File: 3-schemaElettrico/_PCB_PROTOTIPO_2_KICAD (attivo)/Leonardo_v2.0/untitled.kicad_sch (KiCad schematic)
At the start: 0 parts

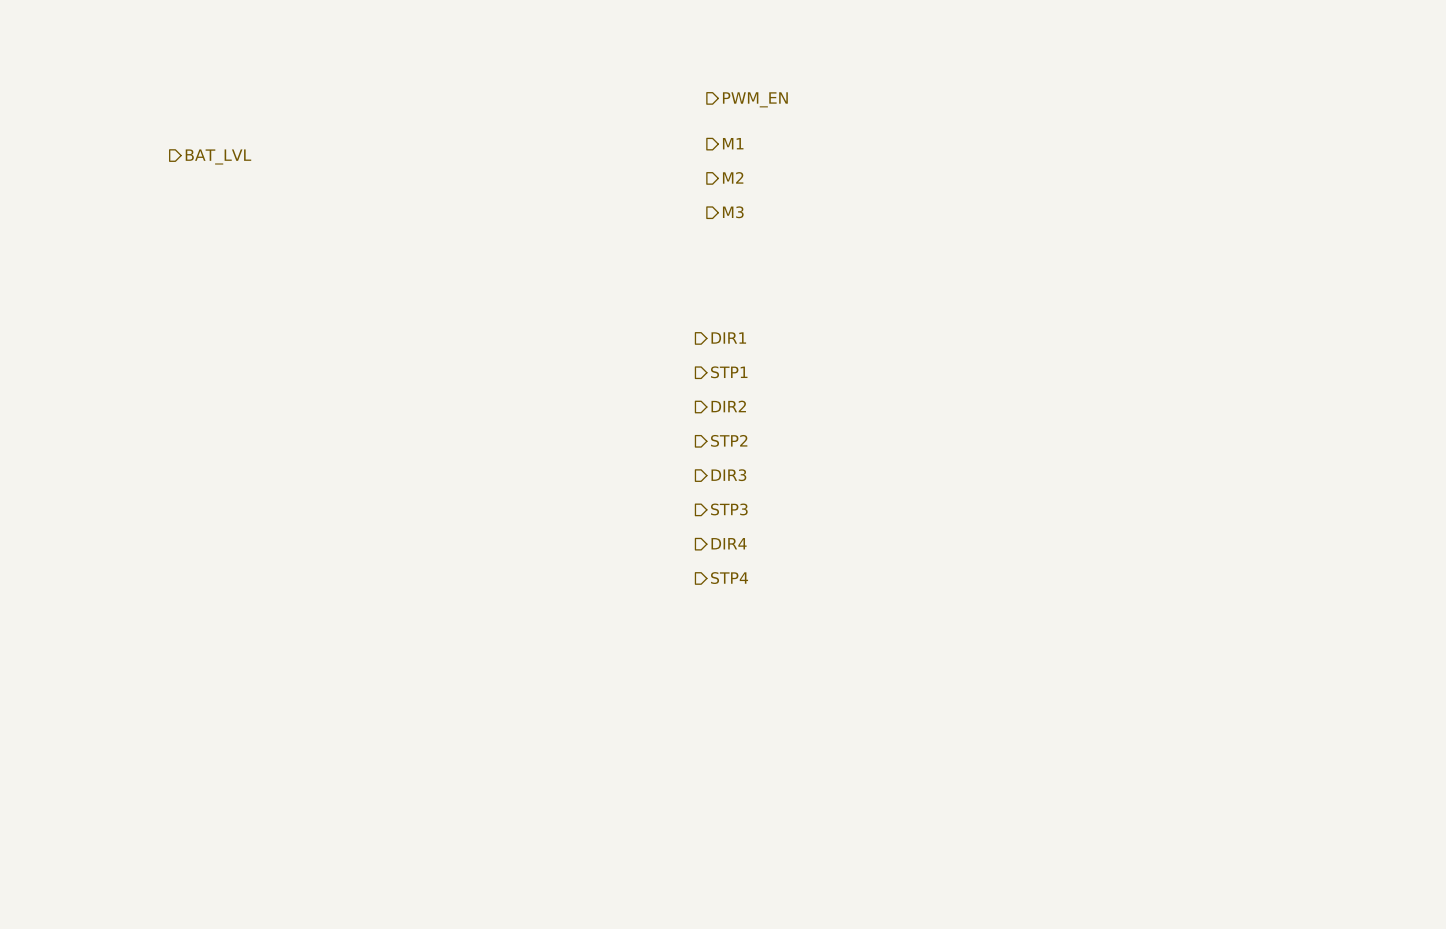
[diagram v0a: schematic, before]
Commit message: placed nodeMCU
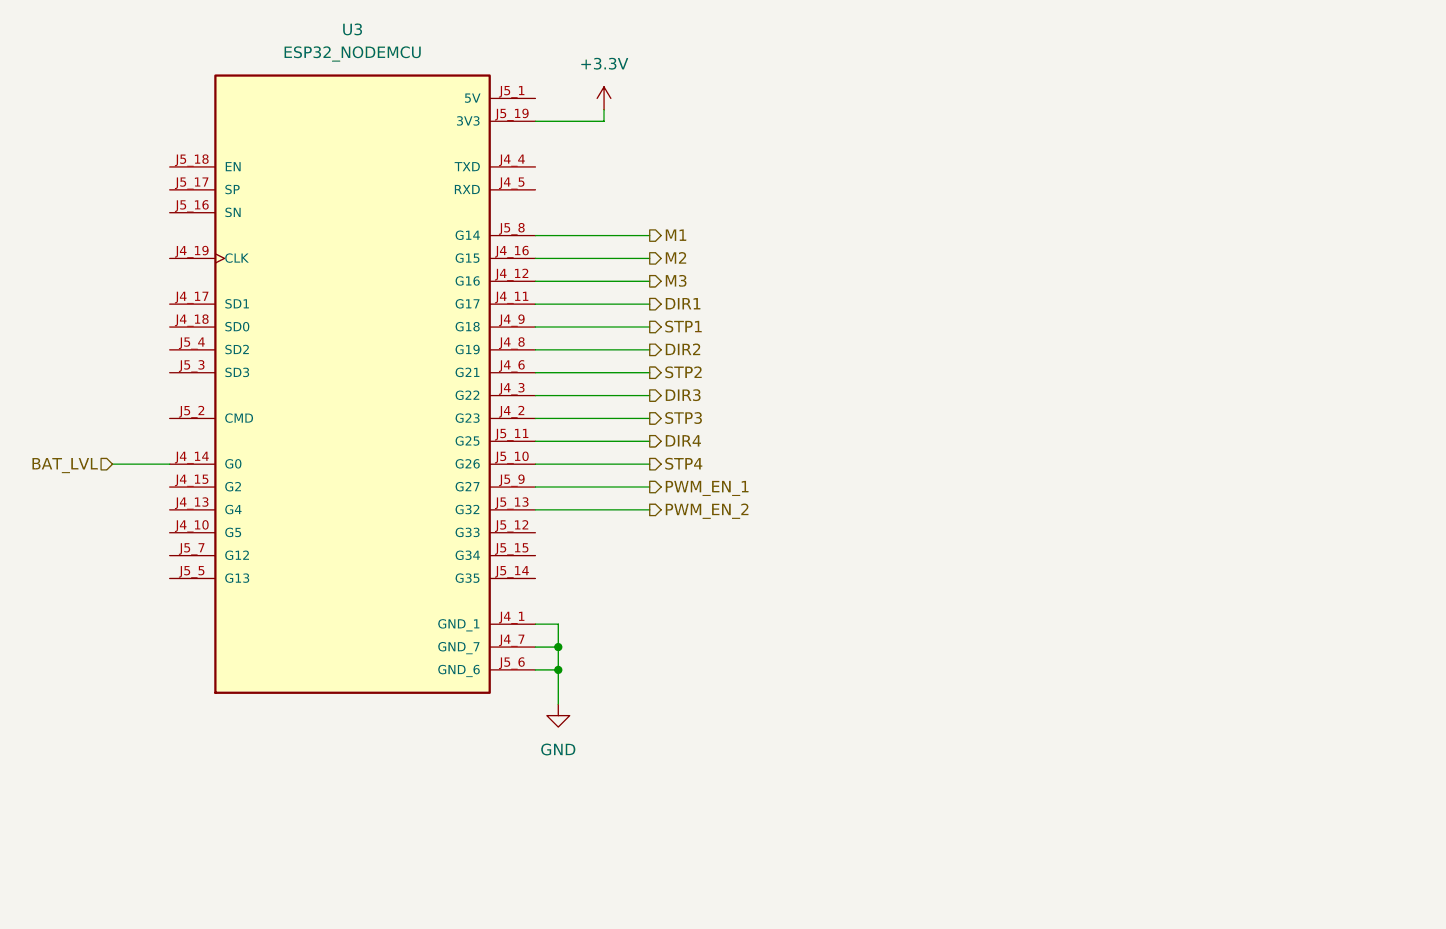
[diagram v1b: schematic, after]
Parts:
- added U3: ESP32_NODEMCU, ESP32_NODEMCU:MODULE_ESP32_NODEMCU, symbol ESP32_NODEMCU:ESP32_NODEMCU
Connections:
- net BAT_LVL: now also U3.J4_14 (G0)
- net DIR1: now also U3.J4_11 (G17)
- net DIR2: now also U3.J4_8 (G19)
- net DIR3: now also U3.J4_3 (G22)
- net DIR4: now also U3.J5_11 (G25)
- net M1: now also U3.J5_8 (G14)
- net M2: now also U3.J4_16 (G15)
- net M3: now also U3.J4_12 (G16)
- net STP1: now also U3.J4_9 (G18)
- net STP2: now also U3.J4_6 (G21)
- net STP3: now also U3.J4_2 (G23)
- net STP4: now also U3.J5_10 (G26)
- new net +3.3V: U3.J5_19 (3V3)
- new net GND: U3.J4_1 (GND_1), U3.J4_7 (GND_7), U3.J5_6 (GND_6)
- new net PWM_EN_1: U3.J5_9 (G27)
- new net PWM_EN_2: U3.J5_13 (G32)

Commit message: ok
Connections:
- net DIR1: now also U3.J4_8 (G19); no longer U3.J4_11 (G17)
- net DIR2: now also U3.J4_3 (G22); no longer U3.J4_8 (G19)
- net DIR3: now also U3.J5_11 (G25); no longer U3.J4_3 (G22)
- net DIR4: now also U3.J5_9 (G27); no longer U3.J5_11 (G25)
- net M1: now also U3.J4_12 (G16); no longer U3.J5_8 (G14)
- net M2: now also U3.J4_11 (G17); no longer U3.J4_16 (G15)
- net M3: now also U3.J4_9 (G18); no longer U3.J4_12 (G16)
- net PWM_EN_1: now also U3.J5_8 (G14); no longer U3.J5_9 (G27)
- net PWM_EN_2: now also U3.J4_16 (G15); no longer U3.J5_13 (G32)
- net STP1: now also U3.J4_6 (G21); no longer U3.J4_9 (G18)
- net STP2: now also U3.J4_2 (G23); no longer U3.J4_6 (G21)
- net STP3: now also U3.J5_10 (G26); no longer U3.J4_2 (G23)
- net STP4: now also U3.J5_13 (G32); no longer U3.J5_10 (G26)
- net speaker_out: now reaches U3.J4_15 (G2)
- net MS1: now reaches U3.J5_12 (G33)
- net MS3: now reaches U3.J5_14 (G35)
- net MS2: now reaches U3.J5_15 (G34)
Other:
- moved on the sheet: U3

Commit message: ok
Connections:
- net Buzzer: now reaches U3.J4_13 (G4)
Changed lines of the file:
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@@
+	(wire
+		(pts
+			(xy 106.68 109.22) (xy 127 109.22)
+		)
+		(stroke
+			(width 0)
+			(type default)
+		)
+	)
 	(wire
 		(pts
@@
 		)
 	)
+	(global_label "Buzzer"
+		(shape output)
+		(at 106.68 109.22 180)
+		(fields_autoplaced yes)
+		(effects
+			(font
+				(size 1.27 1.27)
+			)
+			(justify right)
+		)
+		(property "Intersheetrefs" "${INTERSHEET_REFS}"
+			(at 97.3448 109.22 0)
+			(effects
+				(font
+					(size 1.27 1.27)
+				)
+				(justify right)
+				(hide yes)
+			)
+		)
+	)

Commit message: semplificato
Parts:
- removed U3: ESP32_NODEMCU, ESP32_NODEMCU:MODULE_ESP32_NODEMCU, symbol ESP32_NODEMCU:ESP32_NODEMCU
- added R6, R7, R8: 10K, symbol Device:R_US
- added SW1: SW_DIP_x03, symbol Switch:SW_DIP_x03
- added U1: ~, symbol LIB_STE:NODEMCU-ESP32-38PIN
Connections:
- net +3.3V: now also R6.2, R7.2, R8.2, U1. (CLK)
- net BAT_LVL: now also U1. (CLK)
- net DIR1: now also U1. (CLK)
- net DIR2: now also U1. (CLK)
- net DIR3: now also U1. (CLK)
- net DIR4: now also U1. (CLK)
- net GND: now also SW1.1, SW1.2, SW1.3, U1. (CLK)
- net M1: now also R6.1, SW1.6
- net M2: now also R7.1, SW1.5
- net M3: now also R8.1, SW1.4
- net PWM_EN_1: now also U1. (CLK)
- net PWM_EN_2: now also U1. (CLK)
- net STP1: now also U1. (CLK)
- net STP2: now also U1. (CLK)
- net STP3: now also U1. (CLK)
- net STP4: now also U1. (CLK)
- new net LED: U1. (CLK)
- new net M1A: U1. (CLK)
- new net M1B: U1. (CLK)
- new net M1C: U1. (CLK)
- new net M1D: U1. (CLK)
- new net M2A: U1. (CLK)
- new net M2B: U1. (CLK)
- new net M2C: U1. (CLK)
- new net M2D: U1. (CLK)
- new net RX: U1. (CLK)
- new net TX: U1. (CLK)
- new net buzzer: U1. (CLK)

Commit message: OK
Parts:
- removed SW1: SW_DIP_x03, symbol Switch:SW_DIP_x03
- added J13: Conn_02x03_Odd_Even, Connector_PinHeader_2.54mm:PinHeader_2x03_P2.54mm_Vertical, symbol Connector_Generic:Conn_02x03_Odd_Even
- R6, R7, R8: footprint (none) -> Resistor_SMD:R_0805_2012Metric
- U1: footprint (none) -> ESP32_NODEMCU:DIP-38_1000_ELL
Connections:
- net +3.3V: now also U1.1 (3v3); no longer U1. (CLK)
- net BAT_LVL: now also U1.6 (G35); no longer U1. (CLK)
- net DIR1: now also U1.30 (G18); no longer U1. (CLK)
- net DIR2: now also U1.28 (G17); no longer U1. (CLK)
- net DIR3: now also U1.26 (G4); no longer U1. (CLK)
- net DIR4: now also U1.24 (G2); no longer U1. (CLK)
- net GND: now also U1.14 (GND), U1.32 (GND), U1.38 (GND), J13.1 (Pin_1), J13.3 (Pin_3), J13.5 (Pin_5); no longer U1. (CLK)
- net LED: now also U1.33 (G21); no longer U1. (CLK)
- net M1: now also R8.1, J13.6 (Pin_6); no longer R6.1
- net M1A: now also U1.7 (G32); no longer U1. (CLK)
- net M1B: now also U1.8 (G33); no longer U1. (CLK)
- net M1C: now also U1.9 (G25); no longer U1. (CLK)
- net M1D: now also U1.10 (G26); no longer U1. (CLK)
- net M2: now also J13.4 (Pin_4)
- net M2A: now also U1.11 (G27); no longer U1. (CLK)
- net M2B: now also U1.12 (G14); no longer U1. (CLK)
- net M2C: now also U1.13 (G12); no longer U1. (CLK)
- net M2D: now also U1.15 (G13); no longer U1. (CLK)
- net M3: now also R6.1, J13.2 (Pin_2); no longer R8.1
- net PWM_EN_1: now also U1.37 (G23); no longer U1. (CLK)
- net PWM_EN_2: now also U1.36 (G22); no longer U1. (CLK)
- net RX: now also U1.34 (RXD); no longer U1. (CLK)
- net STP1: now also U1.29 (G5); no longer U1. (CLK)
- net STP2: now also U1.27 (G16); no longer U1. (CLK)
- net STP3: now also U1.25 (G0); no longer U1. (CLK)
- net STP4: now also U1.23 (G15); no longer U1. (CLK)
- net TX: now also U1.35 (TXD); no longer U1. (CLK)
- net buzzer: now also U1.31 (G19); no longer U1. (CLK)

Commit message: OK
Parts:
- removed J13: Conn_02x03_Odd_Even, Connector_PinHeader_2.54mm:PinHeader_2x03_P2.54mm_Vertical, symbol Connector_Generic:Conn_02x03_Odd_Even
- removed R6, R7, R8: 10K, Resistor_SMD:R_0805_2012Metric, symbol Device:R_US
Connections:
- net BAT_LVL is gone; now on net M1B: U1.6 (G35)
- net M1A: now also U1.5 (G34); no longer U1.7 (G32)
- net M1B: no longer U1.8 (G33)
- net M1C: now also U1.7 (G32); no longer U1.9 (G25)
- net M1D: now also U1.8 (G33); no longer U1.10 (G26)
- net PWM_EN_1: now also U1.9 (G25); no longer U1.37 (G23)
- net PWM_EN_2: now also U1.10 (G26); no longer U1.36 (G22)
- net LED renamed FC2
- net buzzer renamed FC1
- new net FC3: U1.36 (G22)
- new net FC4: U1.37 (G23)
- no-connect marks 0 -> 10

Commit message: ok
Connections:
- net DIR1: now also U1.29 (G5); no longer U1.30 (G18)
- net DIR2: now also U1.27 (G16); no longer U1.28 (G17)
- net DIR3: now also U1.25 (G0); no longer U1.26 (G4)
- net DIR4: now also U1.23 (G15); no longer U1.24 (G2)
- net STP1: now also U1.30 (G18); no longer U1.29 (G5)
- net STP2: now also U1.28 (G17); no longer U1.27 (G16)
- net STP3: now also U1.26 (G4); no longer U1.25 (G0)
- net STP4: now also U1.24 (G2); no longer U1.23 (G15)
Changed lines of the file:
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@@
+	(wire
+		(pts
+			(xy 147.32 113.03) (xy 153.67 113.03)
+		)
+		(stroke
+			(width 0)
+			(type default)
+		)
+	)
+	(wire
+		(pts
+			(xy 147.32 85.09) (xy 153.67 85.09)
+		)
+		(stroke
+			(width 0)
+			(type default)
+		)
+	)
+	(wire
+		(pts
+			(xy 147.32 74.93) (xy 179.07 74.93)
+		)
+		(stroke
+			(width 0)
+			(type default)
+		)
+	)
+	(wire
+		(pts
+			(xy 147.32 102.87) (xy 153.67 102.87)
+		)
+		(stroke
+			(width 0)
+			(type default)
+		)
+	)
+	(wire
+		(pts
+			(xy 92.71 74.93) (xy 92.71 69.85)
+		)
+		(stroke
+			(width 0)
+			(type default)
+		)
+	)
+	(wire
+		(pts
+			(xy 111.76 90.17) (xy 119.38 90.17)
+		)
+		(stroke
+			(width 0)
+			(type default)
+		)
+	)
+	(wire
+		(pts
+			(xy 147.32 100.33) (xy 153.67 100.33)
+		)
+		(stroke
+			(width 0)
+			(type default)
+		)
+	)
+	(wire
+		(pts
+			(xy 179.07 90.17) (xy 179.07 95.25)
+		)
+		(stroke
+			(width 0)
+			(type default)
+		)
+	)
+	(wire
+		(pts
+			(xy 147.32 77.47) (xy 153.67 77.47)
+		)
+		(stroke
+			(width 0)
+			(type default)
+		)
+	)
+	(wire
+		(pts
+			(xy 92.71 109.22) (xy 92.71 107.95)
+		)
+		(stroke
+			(width 0)
+			(type default)
+		)
+	)
+	(wire
+		(pts
+			(xy 147.32 92.71) (xy 153.67 92.71)
+		)
+		(stroke
+			(width 0)
+			(type default)
+		)
+	)
+	(wire
+		(pts
+			(xy 111.76 100.33) (xy 119.38 100.33)
+		)
+		(stroke
+			(width 0)
+			(type default)
+		)
+	)
+	(wire
+		(pts
+			(xy 179.07 74.93) (xy 179.07 90.17)
+		)
+		(stroke
+			(width 0)
+			(type default)
+		)
+	)
+	(wire
+		(pts
+			(xy 147.32 87.63) (xy 153.67 87.63)
+		)
+		(stroke
+			(width 0)
+			(type default)
+		)
+	)
+	(wire
+		(pts
+			(xy 147.32 95.25) (xy 153.67 95.25)
+		)
+		(stroke
+			(width 0)
+			(type default)
+		)
+	)
+	(wire
+		(pts
+			(xy 147.32 107.95) (xy 153.67 107.95)
+		)
+		(stroke
+			(width 0)
+			(type default)
+		)
+	)
+	(wire
+		(pts
+			(xy 111.76 95.25) (xy 119.38 95.25)
+		)
+		(stroke
+			(width 0)
+			(type default)
+		)
+	)
+	(wire
+		(pts
+			(xy 111.76 102.87) (xy 119.38 102.87)
+		)
+		(stroke
+			(width 0)
+			(type default)
+		)
+	)
 	(wire
 		(pts
@@
 	(wire
 		(pts
-			(xy 147.32 85.09) (xy 153.67 85.09)
-		)
-		(stroke
-			(width 0)
-			(type default)
-		)
-	)
-	(wire
-		(pts
-			(xy 147.32 74.93) (xy 179.07 74.93)
-		)
-		(stroke
-			(width 0)
-			(type default)
-		)
-	)
-	(wire
-		(pts
-			(xy 92.71 74.93) (xy 92.71 69.85)
-		)
-		(stroke
-			(width 0)
-			(type default)
-		)
-	)
-	(wire
-		(pts
-			(xy 111.76 90.17) (xy 119.38 90.17)
-		)
-		(stroke
-			(width 0)
-			(type default)
-		)
-	)
-	(wire
-		(pts
-			(xy 179.07 90.17) (xy 179.07 95.25)
+			(xy 111.76 85.09) (xy 119.38 85.09)
 		)
 		(stroke
@@
 	(wire
 		(pts
-			(xy 147.32 77.47) (xy 153.67 77.47)
-		)
-		(stroke
-			(width 0)
-			(type default)
-		)
-	)
-	(wire
-		(pts
-			(xy 147.32 100.33) (xy 153.67 100.33)
-		)
-		(stroke
-			(width 0)
-			(type default)
-		)
-	)
-	(wire
-		(pts
-			(xy 147.32 113.03) (xy 153.67 113.03)
-		)
-		(stroke
-			(width 0)
-			(type default)
-		)
-	)
-	(wire
-		(pts
-			(xy 92.71 109.22) (xy 92.71 107.95)
-		)
-		(stroke
-			(width 0)
-			(type default)
-		)
-	)
-	(wire
-		(pts
-			(xy 147.32 107.95) (xy 153.67 107.95)
-		)
-		(stroke
-			(width 0)
-			(type default)
-		)
-	)
-	(wire
-		(pts
-			(xy 147.32 92.71) (xy 153.67 92.71)
-		)
-		(stroke
-			(width 0)
-			(type default)
-		)
-	)
-	(wire
-		(pts
-			(xy 111.76 100.33) (xy 119.38 100.33)
-		)
-		(stroke
-			(width 0)
-			(type default)
-		)
-	)
-	(wire
-		(pts
-			(xy 179.07 74.93) (xy 179.07 90.17)
-		)
-		(stroke
-			(width 0)
-			(type default)
-		)
-	)
-	(wire
-		(pts
-			(xy 147.32 87.63) (xy 153.67 87.63)
-		)
-		(stroke
-			(width 0)
-			(type default)
-		)
-	)
-	(wire
-		(pts
-			(xy 111.76 95.25) (xy 119.38 95.25)
-		)
-		(stroke
-			(width 0)
-			(type default)
-		)
-	)
-	(wire
-		(pts
-			(xy 147.32 95.25) (xy 153.67 95.25)
-		)
-		(stroke
-			(width 0)
-			(type default)
-		)
-	)
-	(wire
-		(pts
-			(xy 111.76 102.87) (xy 119.38 102.87)
-		)
-		(stroke
-			(width 0)
-			(type default)
-		)
-	)
-	(wire
-		(pts
-			(xy 111.76 85.09) (xy 119.38 85.09)
-		)
-		(stroke
-			(width 0)
-			(type default)
-		)
-	)
-	(wire
-		(pts
 			(xy 111.76 87.63) (xy 119.38 87.63)
 		)
@@
 	(wire
 		(pts
+			(xy 147.32 82.55) (xy 153.67 82.55)
+		)
+		(stroke
+			(width 0)
+			(type default)
+		)
+	)
+	(wire
+		(pts
 			(xy 147.32 110.49) (xy 153.67 110.49)
 		)
@@
 	(wire
 		(pts
-			(xy 147.32 102.87) (xy 153.67 102.87)
-		)
-		(stroke
-			(width 0)
-			(type default)
-		)
-	)
-	(wire
-		(pts
-			(xy 147.32 82.55) (xy 153.67 82.55)
-		)
-		(stroke
-			(width 0)
-			(type default)
-		)
-	)
-	(wire
-		(pts
 			(xy 111.76 105.41) (xy 119.38 105.41)
 		)
@@
 	(hierarchical_label "STP4"
 		(shape output)
-		(at 153.67 113.03 0)
+		(at 153.67 110.49 0)
 		(effects
 			(font
@@
 	(hierarchical_label "DIR2"
 		(shape output)
-		(at 153.67 100.33 0)
+		(at 153.67 102.87 0)
 		(effects
 			(font
@@
 	(hierarchical_label "DIR3"
 		(shape output)
-		(at 153.67 105.41 0)
+		(at 153.67 107.95 0)
 		(effects
 			(font
@@
 	(hierarchical_label "DIR1"
 		(shape output)
-		(at 153.67 95.25 0)
+		(at 153.67 97.79 0)
 		(effects
 			(font
@@
 	(hierarchical_label "DIR4"
 		(shape output)
-		(at 153.67 110.49 0)
+		(at 153.67 113.03 0)
 		(effects
 			(font
@@
 	(hierarchical_label "STP3"
 		(shape output)
-		(at 153.67 107.95 0)
+		(at 153.67 105.41 0)
 		(effects
 			(font
@@
 	(hierarchical_label "STP2"
 		(shape output)
-		(at 153.67 102.87 0)
+		(at 153.67 100.33 0)
 		(effects
 			(font
@@
 	(hierarchical_label "STP1"
 		(shape output)
-		(at 153.67 97.79 0)
-		(effects
-			(font
+		(at 153.67 95.25 0)
+		(effects
+			(font
